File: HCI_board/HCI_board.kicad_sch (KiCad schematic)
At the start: 32 parts, among them J1 MCU Controls, J3 Power, J4 USB Data, J7 DC Motor Terminal, J9 USBC_RECP, SW1 Trigger, SW2 Increment, SW3 Reset, SW4 Decrement, U1 NCP1117, U2 ICM7555xB, U3 DRV8833PWP

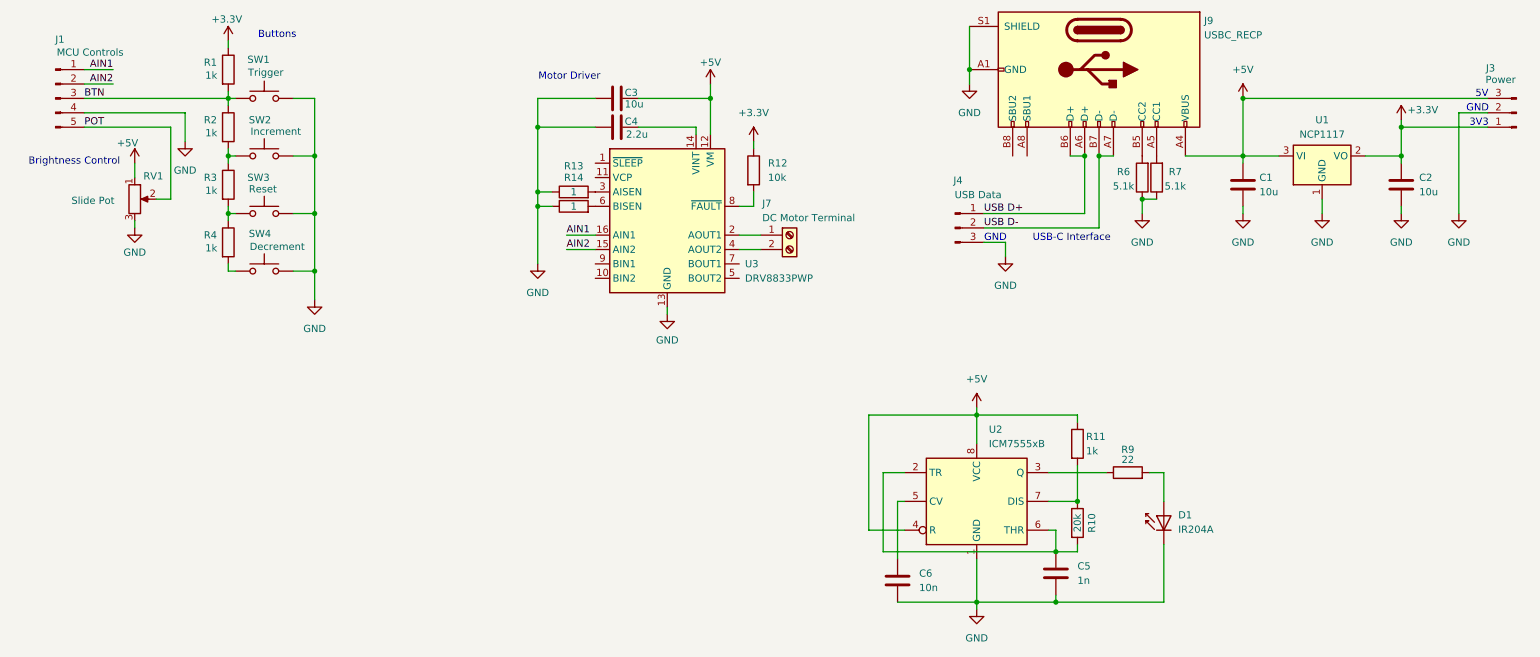
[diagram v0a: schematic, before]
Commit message: removed 555 timer, changed pot from 5v to 3v
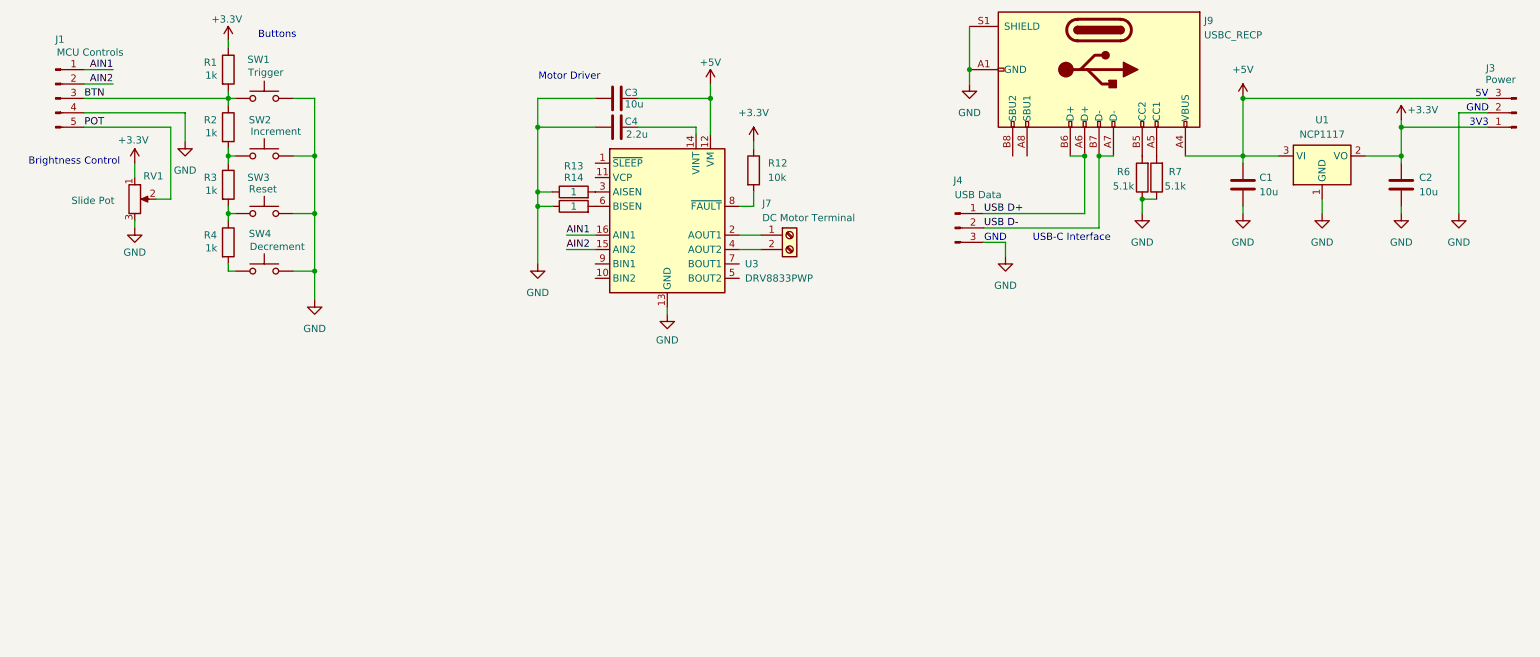
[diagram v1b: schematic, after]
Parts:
- removed C5: 1n, Capacitor_SMD:C_0805_2012Metric, symbol Device:C
- removed C6: 10n, Capacitor_SMD:C_0805_2012Metric, symbol Device:C
- removed D1: IR204A, LED_THT:LED_D3.0mm_IRBlack, symbol LED:IR204A
- removed R10: 20k, Resistor_SMD:R_0805_2012Metric, symbol Device:R
- removed R11: 1k, Resistor_SMD:R_0805_2012Metric, symbol Device:R
- removed R9: 22, Resistor_SMD:R_0805_2012Metric, symbol Device:R
- removed U2: ICM7555xB, Package_SO:SOIC-8_3.9x4.9mm_P1.27mm, symbol Timer:ICM7555xB
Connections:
- net +3.3V: now also RV1.1
- net +5V: no longer RV1.1

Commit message: updated pin configs
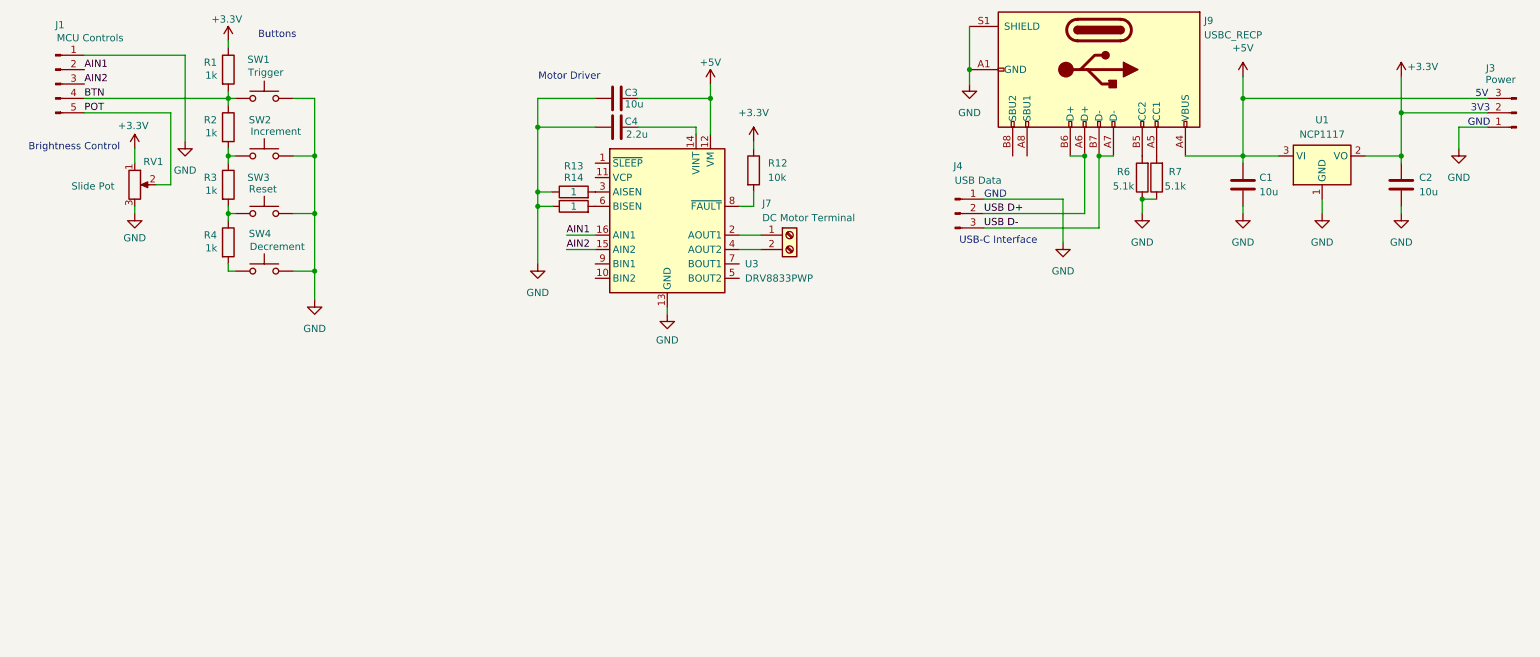
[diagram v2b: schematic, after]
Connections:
- net +3.3V: now also J3.2 (Pin_2); no longer J3.1 (Pin_1)
- net AIN1: now also J1.2 (Pin_2); no longer J1.1 (Pin_1)
- net AIN2: now also J1.3 (Pin_3); no longer J1.2 (Pin_2)
- net BTN: now also J1.4 (Pin_4); no longer J1.3 (Pin_3)
- net GND: now also J1.1 (Pin_1), J3.1 (Pin_1), J4.1 (Pin_1); no longer J1.4 (Pin_4), J3.2 (Pin_2), J4.3 (Pin_3)
- net USB D+: now also J4.2 (Pin_2); no longer J4.1 (Pin_1)
- net USB D-: now also J4.3 (Pin_3); no longer J4.2 (Pin_2)
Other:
- moved on the sheet: J1, J4, RV1

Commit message: added test points
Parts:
- added TP1: GND, TestPoint:TestPoint_Pad_2.0x2.0mm, symbol Connector:TestPoint
- added TP2: 5V, TestPoint:TestPoint_Pad_D2.0mm, symbol Connector:TestPoint
- added TP3: 3V3, TestPoint:TestPoint_Pad_D2.0mm, symbol Connector:TestPoint
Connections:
- net +3.3V: now also TP3.1
- net +5V: now also TP2.1
- net GND: now also TP1.1
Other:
- moved on the sheet: J7

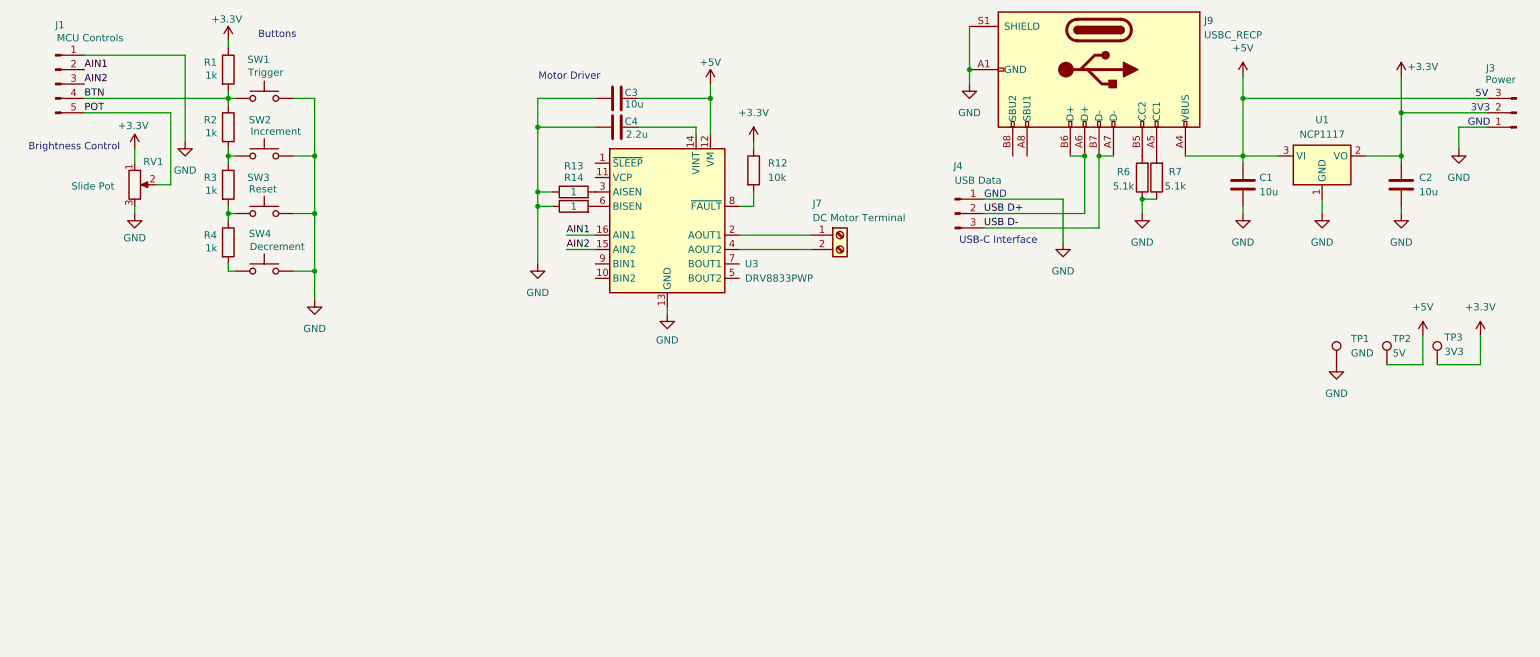
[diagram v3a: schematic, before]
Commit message: Replaced connectors with Clik-Mate Reorganized traces Set planes to both be ground and rerouted power Moved motor driver Organized buttons & slide pot
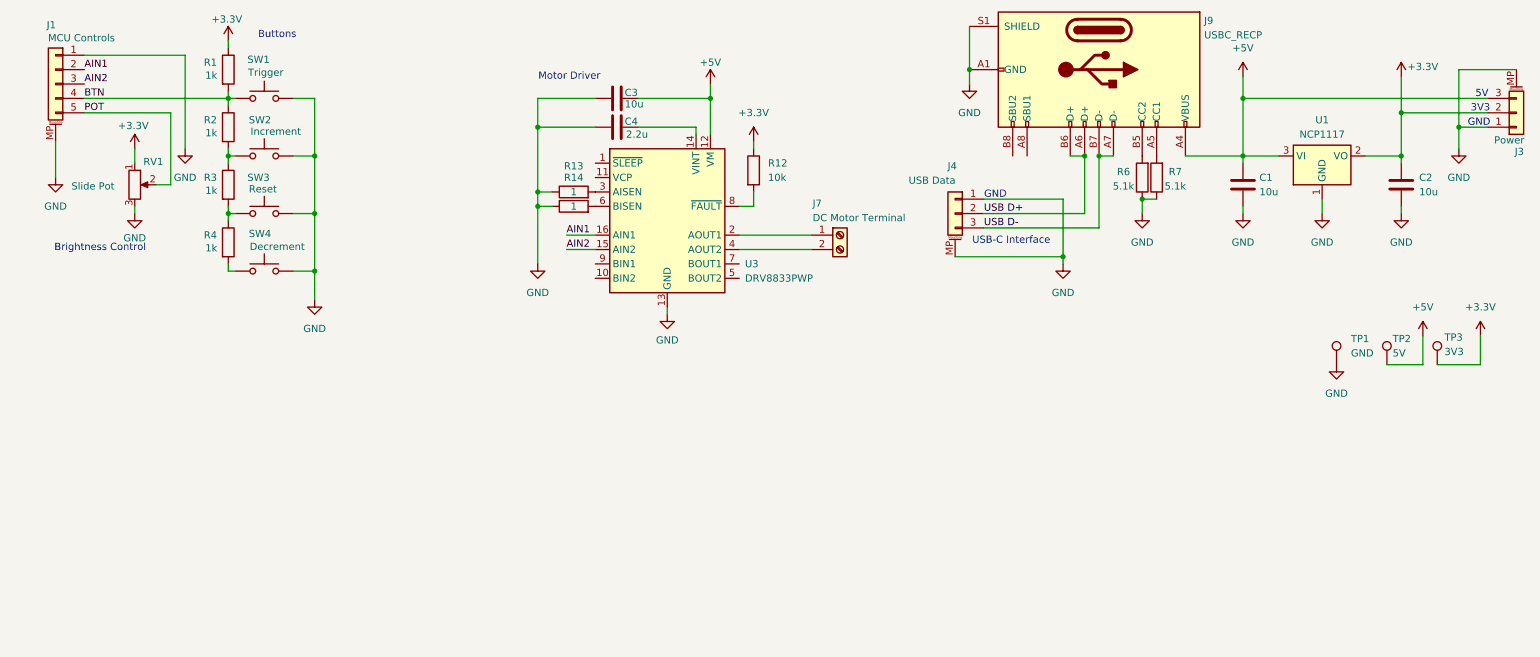
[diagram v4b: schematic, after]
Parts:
- J1: footprint Connector_JST:JST_EH_B5B-EH-A_1x05_P2.50mm_Vertical -> Connector_Molex:Molex_CLIK-Mate_505405-0570_1x05-1MP_P1.50mm_Vertical; symbol Connector:Conn_01x05_Pin -> Connector_Generic_MountingPin:Conn_01x05_MountingPin
- J3, J4: footprint Connector_JST:JST_EH_B3B-EH-A_1x03_P2.50mm_Vertical -> Connector_Molex:Molex_CLIK-Mate_505405-0370_1x03-1MP_P1.50mm_Vertical; symbol Connector:Conn_01x03_Pin -> Connector_Generic_MountingPin:Conn_01x03_MountingPin
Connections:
- net GND: now also J1.MP (MountPin), J3.MP (MountPin), J4.MP (MountPin)
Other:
- moved on the sheet: J3, J4
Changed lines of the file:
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@@
 	(text "USB-C Interface"
 		(exclude_from_sim no)
-		(at 189.23 56.896 0)
+		(at 191.516 56.896 0)
 		(effects
 			(font
@@
 	(text "Brightness Control"
 		(exclude_from_sim no)
-		(at 26.162 40.386 0)
+		(at 30.734 58.166 0)
 		(effects
 			(font
@@
 	)
 	(junction
+		(at 270.51 36.83)
+		(diameter 0)
+		(color 0 0 0 0)
+	)
+	(junction
 		(at 107.95 36.83)
 		(diameter 0)
@@
 	)
 	(junction
+		(at 200.66 59.69)
+		(diameter 0)
+		(color 0 0 0 0)
+	)
+	(junction
 		(at 68.58 62.23)
 		(diameter 0)
@@
 	(wire
 		(pts
+			(xy 280.67 26.67) (xy 270.51 26.67)
+		)
+		(stroke
+			(width 0)
+			(type default)
+		)
+	)
+	(wire
+		(pts
 			(xy 68.58 52.07) (xy 68.58 62.23)
 		)
@@
 	(wire
 		(pts
-			(xy 200.66 57.15) (xy 200.66 49.53)
+			(xy 200.66 60.96) (xy 200.66 59.69)
 		)
 		(stroke
@@
 	(wire
 		(pts
+			(xy 22.86 45.72) (xy 22.86 39.37)
+		)
+		(stroke
+			(width 0)
+			(type default)
+		)
+	)
+	(wire
+		(pts
+			(xy 200.66 59.69) (xy 200.66 49.53)
+		)
+		(stroke
+			(width 0)
+			(type default)
+		)
+	)
+	(wire
+		(pts
 			(xy 270.51 40.64) (xy 270.51 36.83)
 		)
@@
 	(wire
 		(pts
+			(xy 270.51 26.67) (xy 270.51 36.83)
+		)
+		(stroke
+			(width 0)
+			(type default)
+		)
+	)
+	(wire
+		(pts
 			(xy 232.41 41.91) (xy 232.41 31.75)
 		)
@@
 	(wire
 		(pts
+			(xy 181.61 59.69) (xy 200.66 59.69)
+		)
+		(stroke
+			(width 0)
+			(type default)
+		)
+	)
+	(wire
+		(pts
 			(xy 68.58 41.91) (xy 68.58 52.07)
 		)
@@
 	(wire
 		(pts
-			(xy 45.72 24.13) (xy 45.72 39.37)
+			(xy 45.72 24.13) (xy 45.72 40.64)
 		)
 		(stroke
@@
 	)
 	(symbol
-		(lib_id "Connector:Conn_01x03_Pin")
-		(at 280.67 34.29 180)
+		(lib_id "Connector_Generic_MountingPin:Conn_01x03_MountingPin")
+		(at 280.67 34.29 0)
+		(mirror x)
 		(unit 1)
 		(exclude_from_sim no)
@@
 		(dnp no)
 		(property "Reference" "J3"
-			(at 276.098 26.416 0)
+			(at 281.178 41.148 0)
 			(effects
 				(font
@@
 		)
 		(property "Value" "Power"
-			(at 277.876 28.448 0)
+			(at 279.4 39.116 0)
 			(effects
 				(font
@@
 			)
 		)
-		(property "Footprint" "Connector_JST:JST_EH_B3B-EH-A_1x03_P2.50mm_Vertical"
+		(property "Footprint" "Connector_Molex:Molex_CLIK-Mate_505405-0370_1x03-1MP_P1.50mm_Vertical"
 			(at 280.67 34.29 0)
 			(effects
@@
 			)
 		)
-		(property "Description" "Generic connector, single row, 01x03, script generated"
+		(property "Description" "Generic connectable mounting pin connector, single row, 01x03, script generated (kicad-library-utils/schlib/autogen/connector/)"
 			(at 280.67 34.29 0)
 			(effects
@@
 		(pin "3"
 		)
+		(pin "MP"
+		)
 		(instances
 			(project "pill_dispenser_HCI"
@@
 	)
 	(symbol
-		(lib_id "Connector:Conn_01x03_Pin")
+		(lib_id "Connector_Generic_MountingPin:Conn_01x03_MountingPin")
 		(at 181.61 52.07 0)
+		(mirror y)
 		(unit 1)
 		(exclude_from_sim no)
@@
 		(dnp no)
 		(property "Reference" "J4"
-			(at 182.118 43.688 0)
+			(at 181.102 43.688 0)
 			(effects
 				(font
@@
 		)
 		(property "Value" "USB Data"
-			(at 185.674 46.228 0)
+			(at 177.546 46.228 0)
 			(effects
 				(font
@@
 			)
 		)
-		(property "Footprint" "Connector_JST:JST_EH_B3B-EH-A_1x03_P2.50mm_Vertical"
+		(property "Footprint" "Connector_Molex:Molex_CLIK-Mate_505405-0370_1x03-1MP_P1.50mm_Vertical"
 			(at 181.61 52.07 0)
 			(effects
@@
 			)
 		)
-		(property "Description" "Generic connector, single row, 01x03, script generated"
+		(property "Description" "Generic connectable mounting pin connector, single row, 01x03, script generated (kicad-library-utils/schlib/autogen/connector/)"
 			(at 181.61 52.07 0)
 			(effects
@@
 		(pin "3"
 		)
+		(pin "MP"
+		)
 		(instances
 			(project ""
@@
 	)
 	(symbol
+		(lib_id "power:GND")
+		(at 22.86 45.72 0)
+		(unit 1)
+		(exclude_from_sim no)
+		(in_bom yes)
+		(on_board yes)
+		(dnp no)
+		(fields_autoplaced yes)
+		(property "Reference" "#PWR013"
+			(at 22.86 52.07 0)
+			(effects
+				(font
+					(size 1.27 1.27)
+				)
+				(hide yes)
+			)
+		)
+		(property "Value" "GND"
+			(at 22.86 50.8 0)
+			(effects
+				(font
+					(size 1.27 1.27)
+				)
+			)
+		)
+		(property "Footprint" ""
+			(at 22.86 45.72 0)
+			(effects
+				(font
+					(size 1.27 1.27)
+				)
+				(hide yes)
+			)
+		)
+		(property "Datasheet" ""
+			(at 22.86 45.72 0)
+			(effects
+				(font
+					(size 1.27 1.27)
+				)
+				(hide yes)
+			)
+		)
+		(property "Description" "Power symbol creates a global label with name \"GND\" , ground"
+			(at 22.86 45.72 0)
+			(effects
+				(font
+					(size 1.27 1.27)
+				)
+				(hide yes)
+			)
+		)
+		(pin "1"
+		)
+		(instances
+			(project ""
+				(path "/b0029883-bfd8-42a7-87ce-53e4edc8d9ce"
+					(reference "#PWR013")
+					(unit 1)
+				)
+			)
+		)
+	)
+	(symbol
 		(lib_id "Driver_Motor:DRV8833PWP")
 		(at 130.81 53.34 0)
@@
 	)
 	(symbol
-		(lib_id "Connector:Conn_01x05_Pin")
+		(lib_id "Connector_Generic_MountingPin:Conn_01x05_MountingPin")
 		(at 22.86 29.21 0)
+		(mirror y)
 		(unit 1)
 		(exclude_from_sim no)
@@
 		(dnp no)
 		(property "Reference" "J1"
-			(at 23.622 18.796 0)
+			(at 22.098 18.796 0)
 			(effects
 				(font
@@
 		)
 		(property "Value" "MCU Controls"
-			(at 28.956 21.082 0)
+			(at 27.432 21.082 0)
 			(effects
 				(font
@@
 			)
 		)
-		(property "Footprint" "Connector_JST:JST_EH_B5B-EH-A_1x05_P2.50mm_Vertical"
+		(property "Footprint" "Connector_Molex:Molex_CLIK-Mate_505405-0570_1x05-1MP_P1.50mm_Vertical"
 			(at 22.86 29.21 0)
 			(effects
@@
 			)
 		)
-		(property "Description" "Generic connector, single row, 01x05, script generated"
+		(property "Description" "Generic connectable mounting pin connector, single row, 01x05, script generated (kicad-library-utils/schlib/autogen/connector/)"
 			(at 22.86 29.21 0)
 			(effects
@@
 		(pin "3"
 		)
+		(pin "MP"
+		)
 		(instances
 			(project ""
@@
 	(symbol
 		(lib_id "power:GND")
-		(at 45.72 39.37 0)
+		(at 45.72 40.64 0)
 		(unit 1)
 		(exclude_from_sim no)
@@
 		(fields_autoplaced yes)
 		(property "Reference" "#PWR06"
-			(at 45.72 45.72 0)
+			(at 45.72 46.99 0)
 			(effects
 				(font
@@
 		)
 		(property "Value" "GND"
-			(at 45.72 44.45 0)
+			(at 45.72 45.72 0)
 			(effects
 				(font
@@
 		)
 		(property "Footprint" ""
-			(at 45.72 39.37 0)
+			(at 45.72 40.64 0)
 			(effects
 				(font
@@
 		)
 		(property "Datasheet" ""
-			(at 45.72 39.37 0)
+			(at 45.72 40.64 0)
 			(effects
 				(font
@@
 		)
 		(property "Description" "Power symbol creates a global label with name \"GND\" , ground"
-			(at 45.72 39.37 0)
+			(at 45.72 40.64 0)
 			(effects
 				(font
@@
 	(symbol
 		(lib_id "power:GND")
-		(at 200.66 57.15 0)
+		(at 200.66 60.96 0)
 		(unit 1)
 		(exclude_from_sim no)
@@
 		(fields_autoplaced yes)
 		(property "Reference" "#PWR02"
-			(at 200.66 63.5 0)
+			(at 200.66 67.31 0)
 			(effects
 				(font
@@
 		)
 		(property "Value" "GND"
-			(at 200.66 62.23 0)
+			(at 200.66 66.04 0)
 			(effects
 				(font
@@
 		)
 		(property "Footprint" ""
-			(at 200.66 57.15 0)
+			(at 200.66 60.96 0)
 			(effects
 				(font
@@
 		)
 		(property "Datasheet" ""
-			(at 200.66 57.15 0)
+			(at 200.66 60.96 0)
 			(effects
 				(font
@@
 		)
 		(property "Description" "Power symbol creates a global label with name \"GND\" , ground"
-			(at 200.66 57.15 0)
+			(at 200.66 60.96 0)
 			(effects
 				(font

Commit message: Updated connectors to consolidate
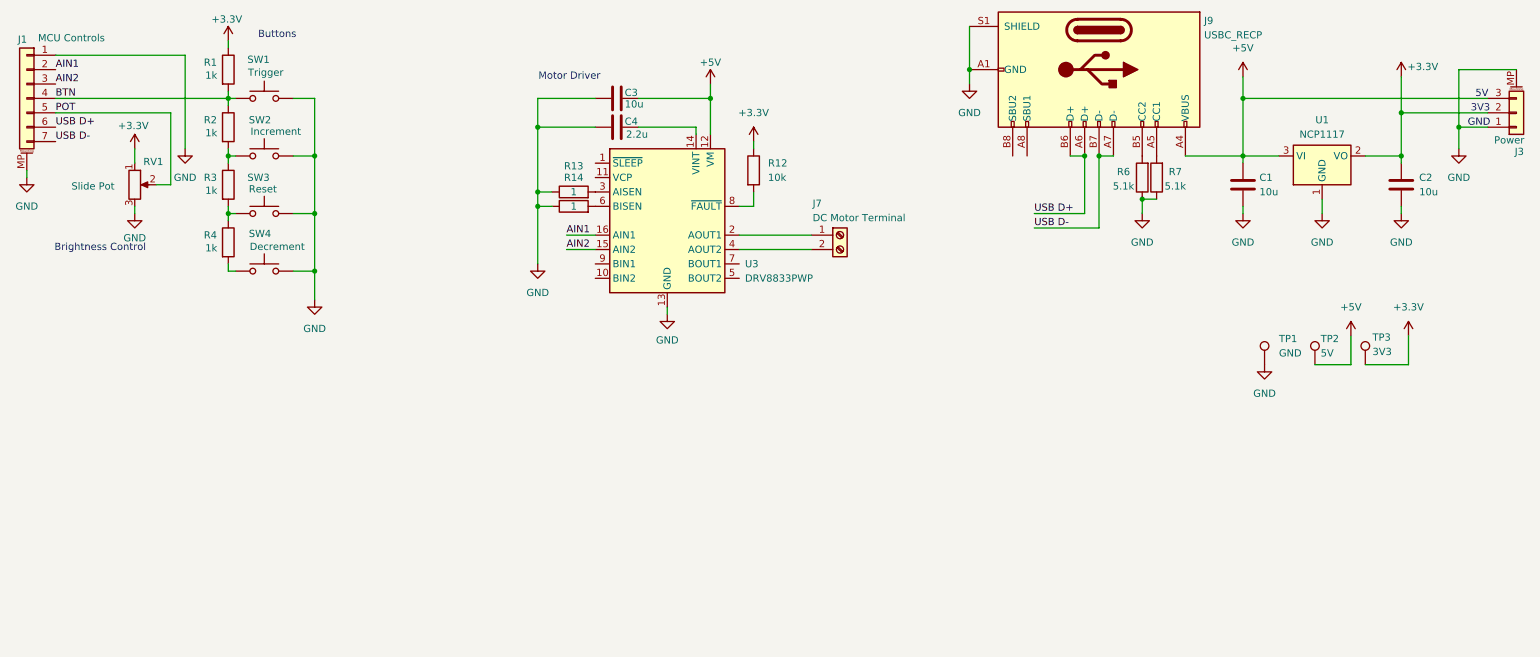
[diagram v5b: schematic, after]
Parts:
- removed J4: USB Data, Connector_Molex:Molex_CLIK-Mate_505405-0370_1x03-1MP_P1.50mm_Vertical, symbol Connector_Generic_MountingPin:Conn_01x03_MountingPin
- J1: footprint Connector_Molex:Molex_CLIK-Mate_505405-0570_1x05-1MP_P1.50mm_Vertical -> Connector_Molex:Molex_CLIK-Mate_505405-0770_1x07-1MP_P1.50mm_Vertical; symbol Connector_Generic_MountingPin:Conn_01x05_MountingPin -> Connector_Generic_MountingPin:Conn_01x07_MountingPin
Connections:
- net USB D+: now also J1.6 (Pin_6)
- net USB D-: now also J1.7 (Pin_7)
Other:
- note removed: "USB-C Interface"
- moved on the sheet: TP1, TP2, TP3
